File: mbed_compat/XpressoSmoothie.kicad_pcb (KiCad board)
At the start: 2 copper layers, 99.7 x 99.7 mm, 116 parts, among them J1 HEADER_4, J10 HEADER_3X2, J11 Pwr_in, J12 HEADER_4, J13 HEADER_4, J14 HEADER_3X2, J15 HEADER_4, J16 HEADER_3, J17 HEADER_3, J18 HEADER_3, J19 HEADER_2, J2 HEADER_4, J20 HEADER_2, J21 HEADER_2, J22 HEADER_2, J23 HEADER_3, J24 HEADER_3, J25 HEADER_3, J26 USB, J27 HEADER_4, J28 MICROSD-MOLEX, J3 HEADER_3, J4 HEADER_3X2, J5 HEADER_3X2, J6 LPCXPRESSO_GENERIC_HEADER, J7 HEADER_4, J8 HEADER_4, J9 HEADER_3X2, M1 LOGO_OSHW, M2 LOGO_OSHW, Q1 IRLB 8743, Q2 IRLB 8743, Q3 IRLB 8743, Q4 IRLB 8743, SW1 SW_PUSH, SW2 SW_PUSH, U1 POLOLU_A4988, U10 TC4422A, U11 TC4422A, U12 LM1117-3.3, U2 POLOLU_A4988, U3 POLOLU_A4988, U4 POLOLU_A4988, U5 POLOLU_A4988, U7 LM7812CT, U8 TC4422A, U9 TC4422A

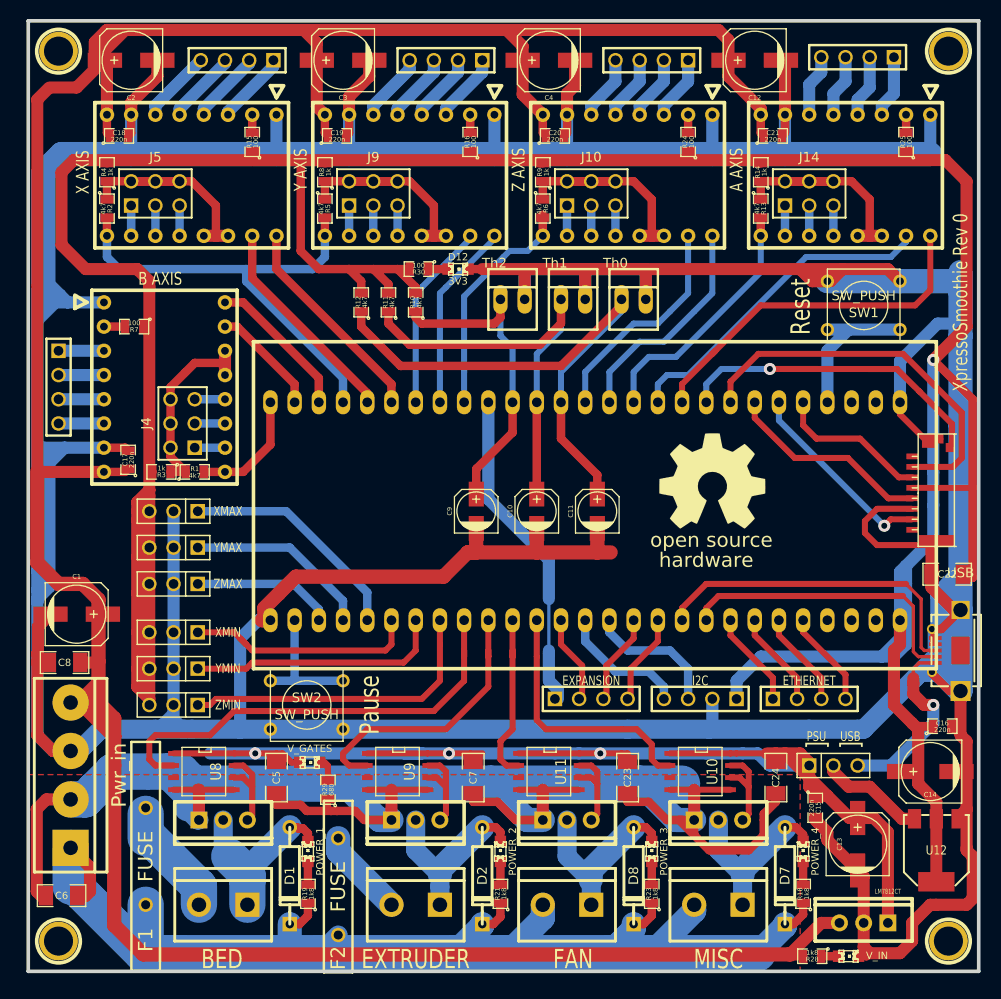
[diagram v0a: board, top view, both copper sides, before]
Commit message: pin alloc mbed compat
pin allocation for mbed compatibility
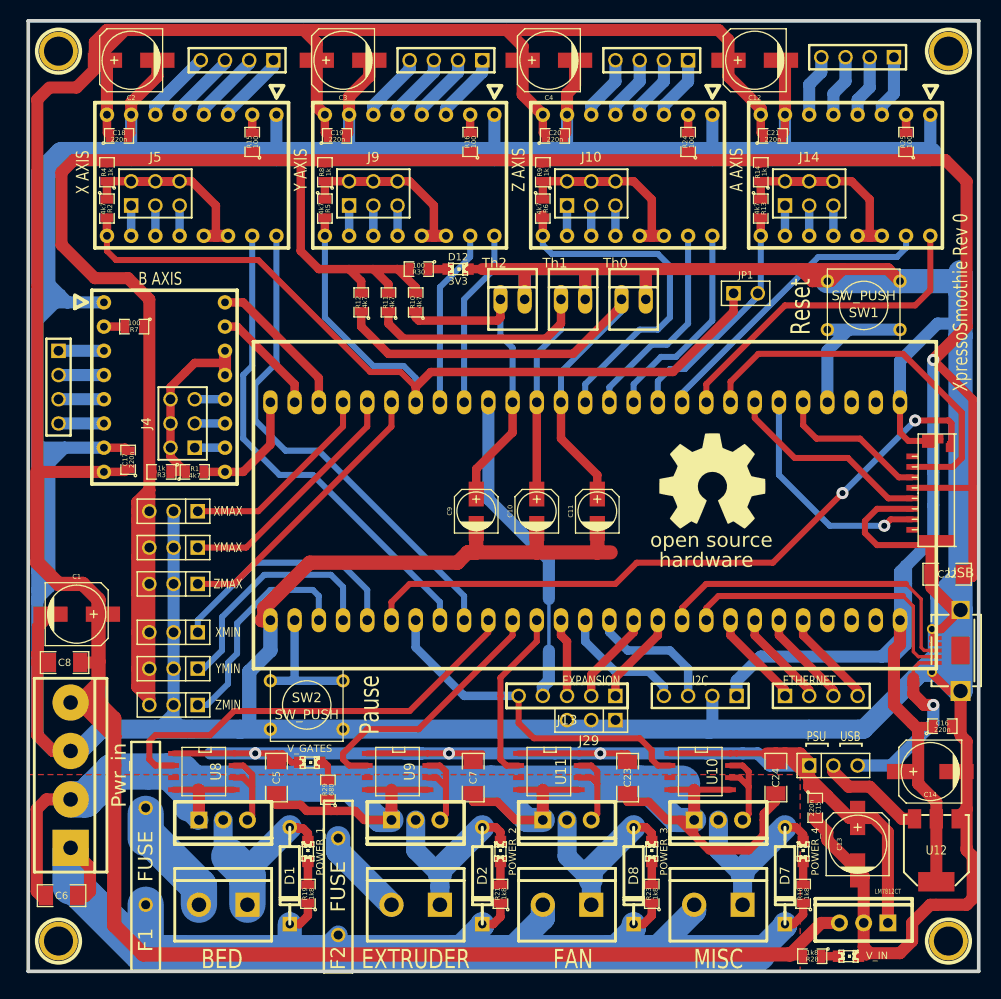
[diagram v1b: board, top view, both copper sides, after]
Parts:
- added J29: HEADER_3, PIN_ARRAY_3X1, F.Cu at (130.8, 127.3)
- added JP1: JUMPER-2, PIN_ARRAY_2X1, F.Cu at (147.0, 82.5)
- J13: value HEADER_4 -> HEADER_5; footprint PIN_ARRAY_4x1 -> PIN_ARRAY_5x1
- moved M1 12.5 mm to (124.5, 91.8)
- moved J13 2.56 mm to (128.3, 124.8), turned to 180 degrees
- moved J27 1.31 mm to (154.9, 124.8)
- moved J15 0.32 mm to (142.2, 124.8)
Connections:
- J13 pad 1: 18_P0.26AOUT -> 38_P0.4CAN
- J13 pad 2: 42_P2.0PWM -> 39_P0.5CAN
- J13 pad 3: 39_P0.5CAN -> 42_P2.0PWM
- J13 pad 4: 38_P0.4CAN -> 18_P0.26AOUT
- J6 pad 10: A-DIR -> A-STEP
- J6 pad 11: A-STEP -> A-EN
- J6 pad 12: A-EN -> Z-DIR
- J6 pad 13: Z-DIR -> Z-STEP
- J6 pad 14: Z-STEP -> Z-EN
- J6 pad 19: Z-EN -> Y-DIR
- J6 pad 20: Y-DIR -> Y-STEP
- J6 pad 21: Y-STEP -> X-EN
- J6 pad 22: X-DIR -> ZMAX
- J6 pad 23: X-STEP -> YMAX
- J6 pad 24: X-EN -> XMAX
- J6 pad 43: POWER4 -> POWER3
- J6 pad 44: POWER3 -> POWER2
- J6 pad 45: POWER2 -> POWER1
- J6 pad 46: POWER1 -> X-DIR
- J6 pad 47: ZMIN -> X-STEP
- J6 pad 48: YMIN -> POWER4
- J6 pad 49: XMIN -> SD_card_detect
- J6 pad 50: XMAX -> XMIN
- J6 pad 51: YMAX -> YMIN
- J6 pad 52: ZMAX -> ZMIN
- J6 pad 9: SD_card_detect -> A-DIR
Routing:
- net X-EN: track 50.3 -> 108.7 mm
- net SD_card_detect: track 33.3 -> 71.3 mm, vias 1 -> 2
- net X-DIR: track 22.5 -> 52.4 mm
- net X-STEP: track 22.5 -> 51.3 mm
- net ZMAX: track 14.9 -> 29.7 mm
- net Z-EN: track 24.2 -> 36.5 mm
- net POWER4: track 27.4 -> 36.9 mm
- net ZMIN: track 32.8 -> 24.0 mm
- net YMAX: track 19.6 -> 25.6 mm
- net MISO: track 20.7 -> 24.1 mm
- net A-DIR: track 38.2 -> 35.2 mm
- net XMAX: track 24.2 -> 21.5 mm
- net A-STEP: track 34.8 -> 32.0 mm
- net Z-DIR: track 23.4 -> 21.8 mm
- net Z-STEP: track 23.4 -> 21.8 mm
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
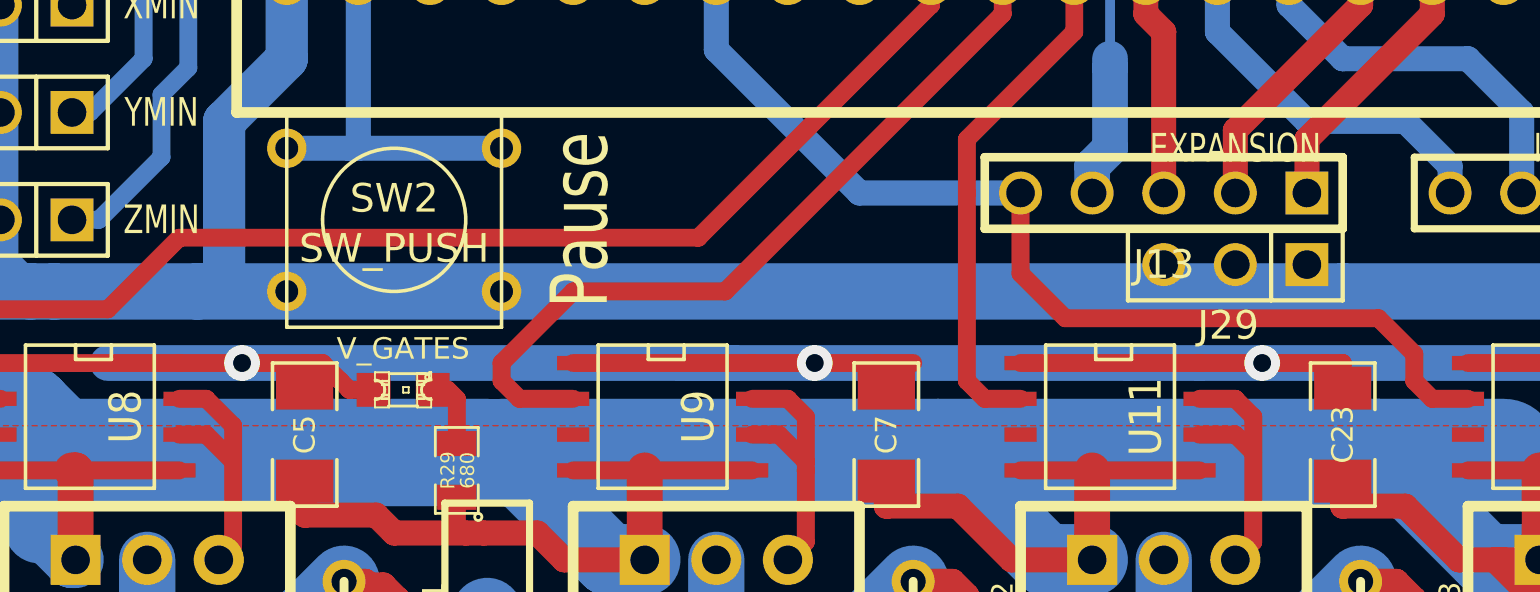
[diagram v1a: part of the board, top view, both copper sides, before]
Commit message: expansion 4gnd
plus 1 gnd pin for expansion
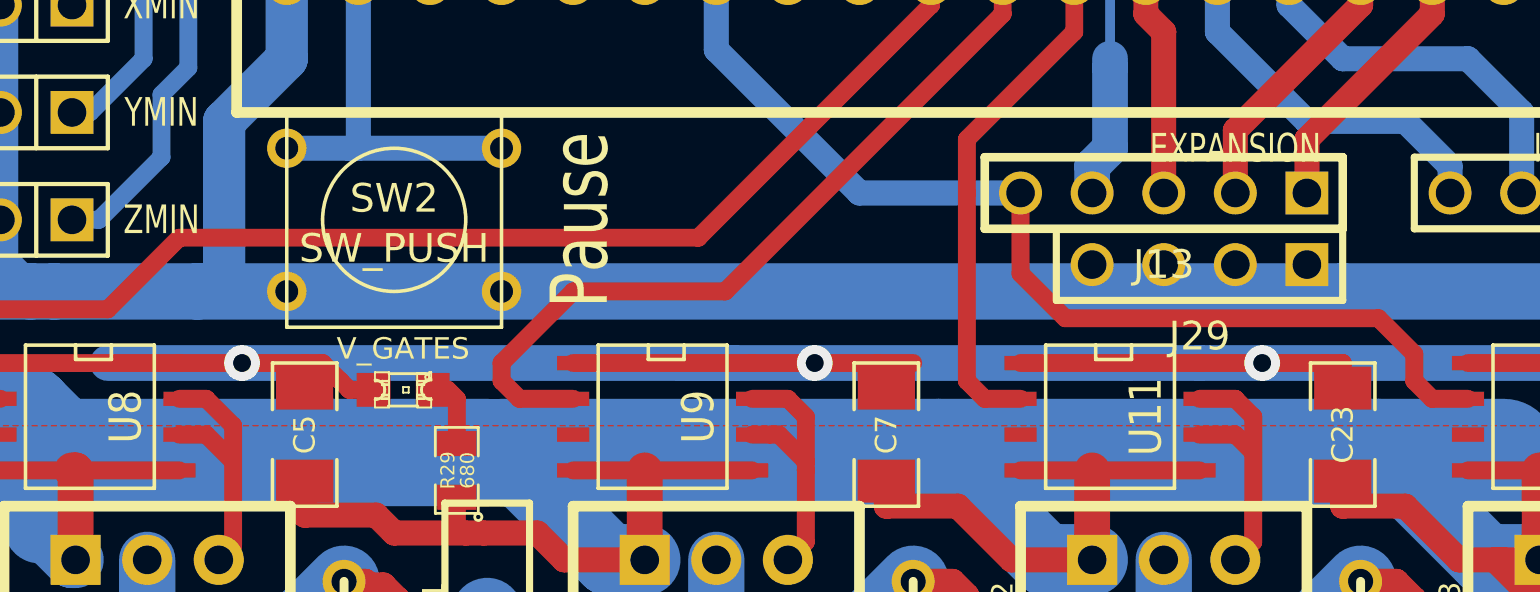
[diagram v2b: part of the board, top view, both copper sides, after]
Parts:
- J29: value HEADER_3 -> HEADER_4; footprint PIN_ARRAY_3X1 -> PIN_ARRAY_4x1
- moved J29 1.27 mm to (129.5, 127.3)
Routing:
- net GND: track 795.0 -> 798.8 mm

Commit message: mos4 pwm fix
mos 4 pwm
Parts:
- removed J29: HEADER_4, PIN_ARRAY_4x1
- added JP2: JUMPER-2, PIN_ARRAY_2X1, F.Cu at (147.0, 82.5)
- J13: value HEADER_5 -> HEADER_4X2; footprint PIN_ARRAY_5x1 -> pin_array_4x2
- moved JP1 52.8 mm to (115.3, 124.8), turned to 180 degrees
- moved J13 1.80 mm to (129.5, 126.0)
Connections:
- J13 pad 2: 39_P0.5CAN -> GND
- J13 pad 3: 42_P2.0PWM -> 39_P0.5CAN
- J13 pad 4: 18_P0.26AOUT -> GND
- J13 pad 5: POWER4 -> 42_P2.0PWM
- J6 pad 43: POWER3 -> POWER4
- J6 pad 44: POWER2 -> POWER3
- J6 pad 45: POWER1 -> POWER2
- J6 pad 48: POWER4 -> POWER1
- JP1 pad 1: X-EN -> 18_P0.26AOUT
- JP1 pad 2: A-EN -> POWER1
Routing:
- net 18_P0.26AOUT: track 34.0 -> 43.9 mm
- net POWER4: track 36.9 -> 29.8 mm
- net POWER2: track 27.9 -> 29.9 mm
- net POWER3: track 18.4 -> 17.3 mm

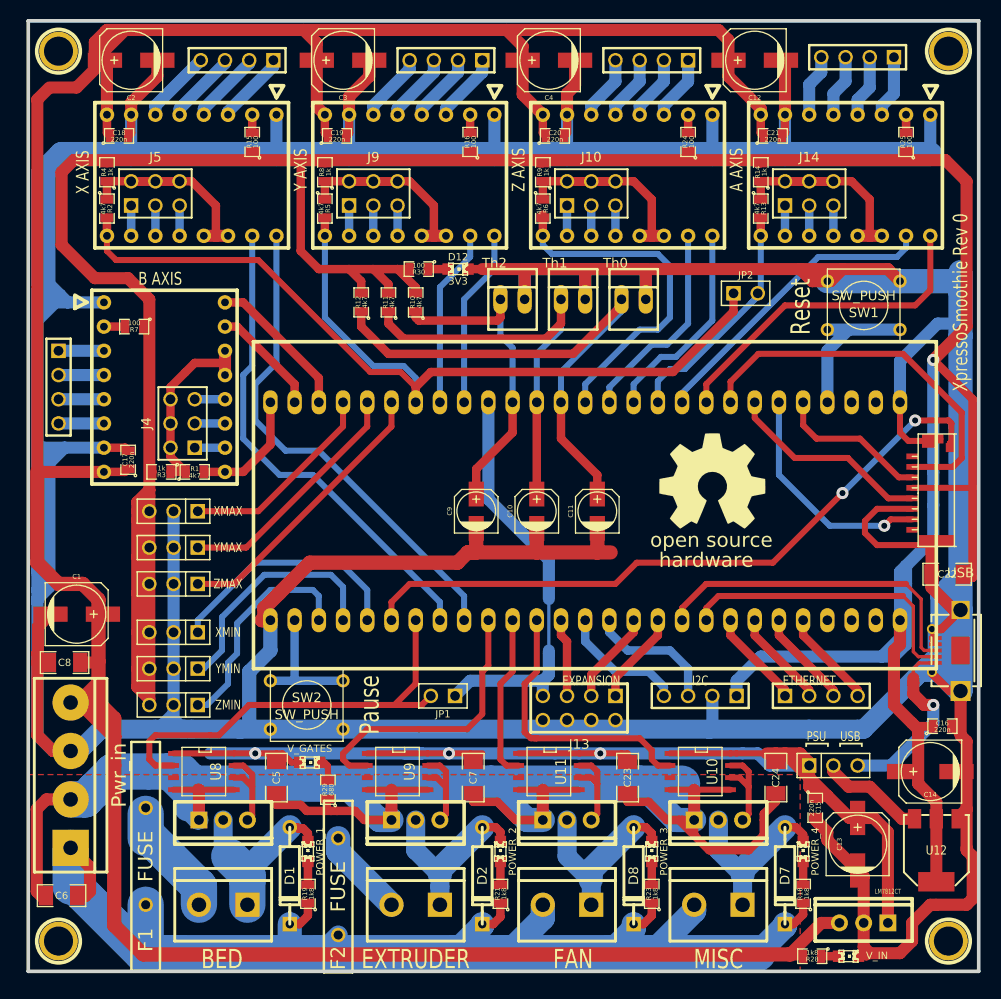
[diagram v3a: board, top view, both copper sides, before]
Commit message: Attempting to add jumpers for mbed-compatible board.
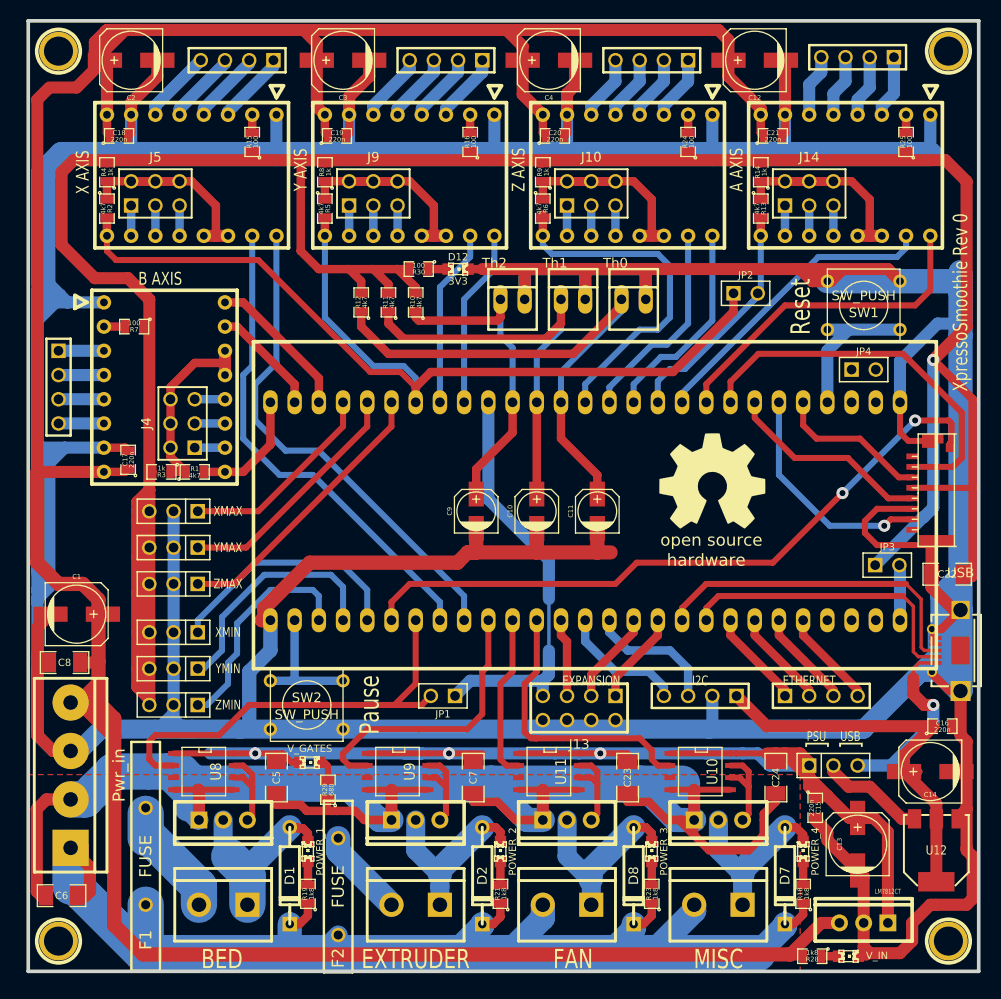
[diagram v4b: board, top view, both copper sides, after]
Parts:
- added JP3: JUMPER-2, PIN_ARRAY_2X1, F.Cu at (161.9, 111.1)
- added JP4: JUMPER-2, PIN_ARRAY_2X1, F.Cu at (159.4, 90.6)
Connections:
- C14 pad 1: VIO3V3 -> VCC
- C16 pad 1: VIO3V3 -> VCC
- C22 pad 1: VIO3V3 -> VCC
- Hole1 pad 1: (no net) -> N-00000132
- Hole2 pad 1: (no net) -> N-00000131
- Hole3 pad 1: (no net) -> N-00000130
- Hole4 pad 1: (no net) -> N-00000129
- J15 pad 1: VIO3V3 -> VCC
- J16 pad 3: VIO3V3 -> VCC
- J17 pad 3: VIO3V3 -> VCC
- J18 pad 3: VIO3V3 -> VCC
- J23 pad 3: VIO3V3 -> VCC
- J24 pad 3: VIO3V3 -> VCC
- J25 pad 3: VIO3V3 -> VCC
- J28 pad 1: (no net) -> N-0000044
- J28 pad 4: VIO3V3 -> VCC
- J28 pad 8: (no net) -> N-0000042
- J6 pad 2: (no net) -> 5VIN
- J6 pad 28: VIO3V3 -> 3V3IN
- J6 pad 29: (no net) -> N-00000124
- J6 pad 3: (no net) -> N-00000127
- J6 pad 30: (no net) -> N-00000126
- J6 pad 31: (no net) -> N-00000125
- R10 pad 2: VIO3V3 -> VCC
- R11 pad 2: VIO3V3 -> VCC
- R12 pad 2: VIO3V3 -> VCC
- R14 pad 2: VIO3V3 -> VCC
- R15 pad 1: VIO3V3 -> VCC
- R16 pad 1: VIO3V3 -> VCC
- R24 pad 1: VIO3V3 -> VCC
- R25 pad 1: VIO3V3 -> VCC
- R3 pad 2: VIO3V3 -> VCC
- R30 pad 2: VIO3V3 -> VCC
- R4 pad 2: VIO3V3 -> VCC
- R7 pad 1: VIO3V3 -> VCC
- R8 pad 2: VIO3V3 -> VCC
- R9 pad 2: VIO3V3 -> VCC
- U10 pad 3: (no net) -> N-0000057
- U11 pad 3: (no net) -> N-0000054
- U12 pad 2: VIO3V3 -> VCC
- U8 pad 3: (no net) -> N-0000037
- U9 pad 3: (no net) -> N-0000055
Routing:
- net VIO3V3: track 405.0 -> 0.00 mm, vias 1 -> 0
- net VCC: track 0.00 -> 373.3 mm, vias 0 -> 1
- net 3V3IN: track 0.00 -> 5.80 mm

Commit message: Finished setting up jumpers and laying power traces for mbed-compatible.
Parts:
- moved JP4 0.18 mm to (159.5, 90.7)
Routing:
- net +5V: track 19.5 -> 72.1 mm, vias 1 -> 3
- net VCC: track 373.3 -> 398.7 mm
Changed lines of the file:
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@@
   (general
     (links 324)
-    (no_connects 14)
-    (area 71.564499 53.784499 171.640501 153.860501)
+    (no_connects 12)
+    (area 56.388 52.51262 179.864657 163.2712)
     (thickness 1.6)
     (drawings 31)
-    (tracks 1105)
+    (tracks 1130)
     (zones 0)
     (modules 120)
@@
   )
   (module PIN_ARRAY_2X1 (layer F.Cu)
-    (at 159.385 90.551)
+    (at 159.512 90.678)
     (descr "Connecteurs 2 pins")
     (tags "CONN DEV")
@@
     (arrow2b (pts (xy 64.770001 53.975) (xy 65.356421 55.101503)))
   )
+  (segment (start 146.685 92.329) (end 147.701 91.313) (width 1.27) (layer B.Cu) (net 1))
+  (segment (start 156.7815 114.7445) (end 156.7815 113.157) (width 1.27) (layer B.Cu) (net 1))
+  (segment (start 162.78098 121.31548) (end 158.84398 121.31548) (width 1.27) (layer F.Cu) (net 1))
+  (segment (start 156.7815 119.253) (end 156.7815 118.618) (width 1.27) (layer B.Cu) (net 1))
+  (segment (start 157.48 119.9515) (end 156.7815 119.253) (width 1.27) (layer B.Cu) (net 1))
+  (via (at 157.48 119.9515) (size 1.27) (layers F.Cu B.Cu) (net 1))
+  (segment (start 158.84398 121.31548) (end 157.48 119.9515) (width 1.27) (layer F.Cu) (net 1))
+  (segment (start 156.7815 114.7445) (end 156.7815 118.618) (width 0.35) (layer B.Cu) (net 1))
+  (segment (start 146.685 103.0605) (end 146.685 96.3295) (width 1.27) (layer B.Cu) (net 1))
+  (segment (start 156.7815 113.157) (end 146.685 103.0605) (width 1.27) (layer B.Cu) (net 1))
+  (segment (start 146.685 92.329) (end 146.685 96.3295) (width 0.35) (layer B.Cu) (net 1))
+  (segment (start 152.9715 90.678) (end 158.242 90.678) (width 1.27) (layer F.Cu) (net 1))
+  (segment (start 152.4 91.2495) (end 152.9715 90.678) (width 1.27) (layer F.Cu) (net 1))
+  (via (at 152.4 91.2495) (size 1.27) (layers F.Cu B.Cu) (net 1))
+  (segment (start 152.3365 91.313) (end 152.4 91.2495) (width 1.27) (layer B.Cu) (net 1))
+  (segment (start 147.701 91.313) (end 152.3365 91.313) (width 1.27) (layer B.Cu) (net 1))
+  (segment (start 165.19652 121.31548) (end 162.78098 121.31548) (width 0.35) (layer F.Cu) (net 1))
+  (segment (start 162.78098 121.31548) (end 162.7505 121.285) (width 0.35) (layer F.Cu) (net 1))
   (segment (start 166.6875 127.635) (end 162.2425 132.08) (width 1.27) (layer B.Cu) (net 1))
   (segment (start 164.592 124.587) (end 165.735 125.73) (width 1.27) (layer F.Cu) (net 1))
@@
   (segment (start 135.255 118.11) (end 130.81 122.555) (width 0.889) (layer F.Cu) (net 8))
   (segment (start 135.255 118.11) (end 135.255 116.84) (width 0.889) (layer F.Cu) (net 8))
-  (segment (start 163.195 116.84) (end 163.195 111.125) (width 1.27) (layer B.Cu) (net 9) (status C00000))
-  (segment (start 163.195 111.125) (end 163.1315 111.0615) (width 1.27) (layer B.Cu) (net 9) (status C00000))
+  (segment (start 163.195 116.84) (end 163.195 111.125) (width 1.27) (layer B.Cu) (net 9))
+  (segment (start 163.195 111.125) (end 163.1315 111.0615) (width 1.27) (layer B.Cu) (net 9))
   (segment (start 128.27 124.7775) (end 128.27 119.0625) (width 0.889) (layer F.Cu) (net 10))
   (segment (start 127.635 118.4275) (end 128.27 119.0625) (width 0.889) (layer F.Cu) (net 10))
@@
   (segment (start 144.145 114.3) (end 163.5125 114.3) (width 0.635) (layer F.Cu) (net 114))
   (segment (start 142.875 115.57) (end 144.145 114.3) (width 0.635) (layer F.Cu) (net 114))
+  (segment (start 159.385 118.618) (end 159.385 121.158) (width 1.27) (layer B.Cu) (net 115))
+  (segment (start 160.5915 113.3475) (end 159.385 114.554) (width 1.27) (layer B.Cu) (net 115))
+  (segment (start 160.5915 111.0615) (end 160.5915 113.3475) (width 1.27) (layer B.Cu) (net 115))
+  (segment (start 159.385 118.618) (end 159.385 114.554) (width 0.35) (layer B.Cu) (net 115))
+  (segment (start 148.3995 122.428) (end 146.05 124.7775) (width 1.27) (layer B.Cu) (net 115) (status 800000))
+  (segment (start 158.115 122.428) (end 148.3995 122.428) (width 1.27) (layer B.Cu) (net 115))
+  (segment (start 159.385 121.158) (end 158.115 122.428) (width 1.27) (layer B.Cu) (net 115))
   (segment (start 160.5915 111.0615) (end 165.608 106.045) (width 1.27) (layer B.Cu) (net 115))
   (via (at 166.6875 89.535) (size 1.27) (layers F.Cu B.Cu) (net 115))
@@
   (segment (start 165.608 106.045) (end 165.6715 106.045) (width 1.27) (layer B.Cu) (net 115))
   (segment (start 166.6875 127.9525) (end 160.655 127.9525) (width 1.27) (layer F.Cu) (net 115))
-  (segment (start 160.655 127.9525) (end 149.225 127.9525) (width 1.27) (layer F.Cu) (net 115))
   (segment (start 149.225 127.9525) (end 146.05 124.7775) (width 1.27) (layer F.Cu) (net 115))
+  (segment (start 160.655 127.9525) (end 149.225 127.9525) (width 1.27) (layer F.Cu) (net 115))
   (segment (start 163.61918 132.715) (end 163.61918 131.02082) (width 1.27) (layer F.Cu) (net 115))
   (segment (start 163.61918 131.02082) (end 166.6875 127.9525) (width 1.27) (layer F.Cu) (net 115))

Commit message: Fixed the 5V trace on the board.
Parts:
- removed JP4: JUMPER-2, PIN_ARRAY_2X1
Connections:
- J6 pad 2: 5VIN -> +5V
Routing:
- net +5V: track 72.1 -> 76.6 mm
